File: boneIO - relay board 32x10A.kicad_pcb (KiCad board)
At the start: 2 copper layers, 197 x 102 mm, 120 parts, among them J1 Screw_Terminal_01x03, J10 Screw_Terminal_01x03, J11 Screw_Terminal_01x03, J12 Conn_02x04_Odd_Even, J13 Screw_Terminal_01x03, J14 Screw_Terminal_01x03, J15 Screw_Terminal_01x03, J16 Screw_Terminal_01x03, J17 Screw_Terminal_01x03, J2 Screw_Terminal_01x03, J3 Screw_Terminal_01x03, J4 Screw_Terminal_01x03, J5 Screw_Terminal_01x03, J6 Screw_Terminal_01x03, J7 Screw_Terminal_01x03, J8 Screw_Terminal_01x03, J9 Screw_Terminal_01x03, K1 HF32F/024-ZS3, K10 HF32F/024-ZS3, K11 HF32F/024-ZS3, K12 HF32F/024-ZS3, K13 HF32F/024-ZS3, K14 HF32F/024-ZS3, K15 HF32F/024-ZS3, K16 HF32F/024-ZS3, K17 HF32F/024-ZS3, K18 HF32F/024-ZS3, K19 HF32F/024-ZS3, K2 HF32F/024-ZS3, K20 HF32F/024-ZS3, K21 HF32F/024-ZS3, K22 HF32F/024-ZS3, K23 HF32F/024-ZS3, K24 HF32F/024-ZS3, K25 HF32F/024-ZS3, K26 HF32F/024-ZS3, K27 HF32F/024-ZS3, K28 HF32F/024-ZS3, K29 HF32F/024-ZS3, K3 HF32F/024-ZS3, K30 HF32F/024-ZS3, K31 HF32F/024-ZS3, K32 HF32F/024-ZS3, K4 HF32F/024-ZS3, K5 HF32F/024-ZS3, K6 HF32F/024-ZS3, K7 HF32F/024-ZS3, K8 HF32F/024-ZS3, K9 HF32F/024-ZS3, SW1 SW_DIP_x03, SW2 SW_DIP_x03, SW3 SW_DIP_x03, U1 PCF8575, U10 LM75_MSOP, U2 ULN2803A, U3 MCP23017_SS, U4 ULN2803A, U5 PCF8575, U6 ULN2803A, U7 MCP23017_SS, U8 ULN2803A, U9 MCP9808_SO8

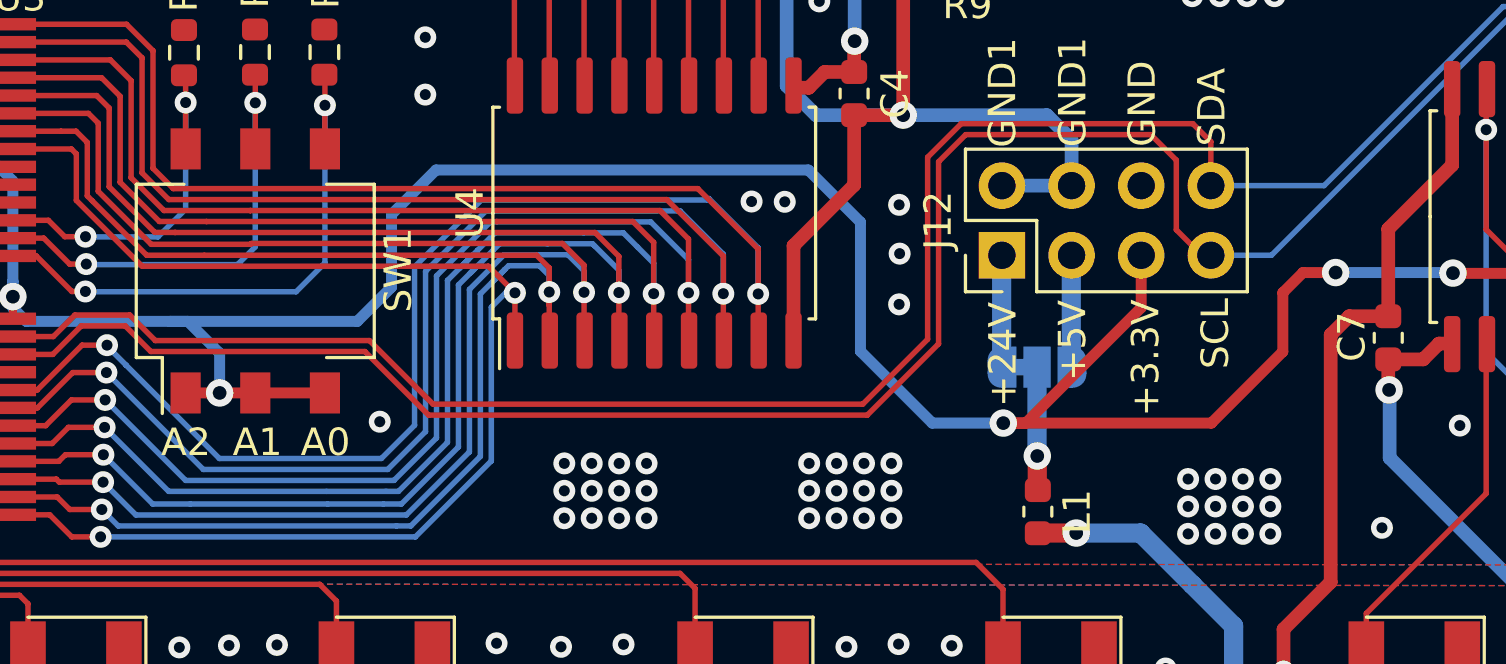
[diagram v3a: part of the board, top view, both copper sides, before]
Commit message: relay board 32x10A
Final Version
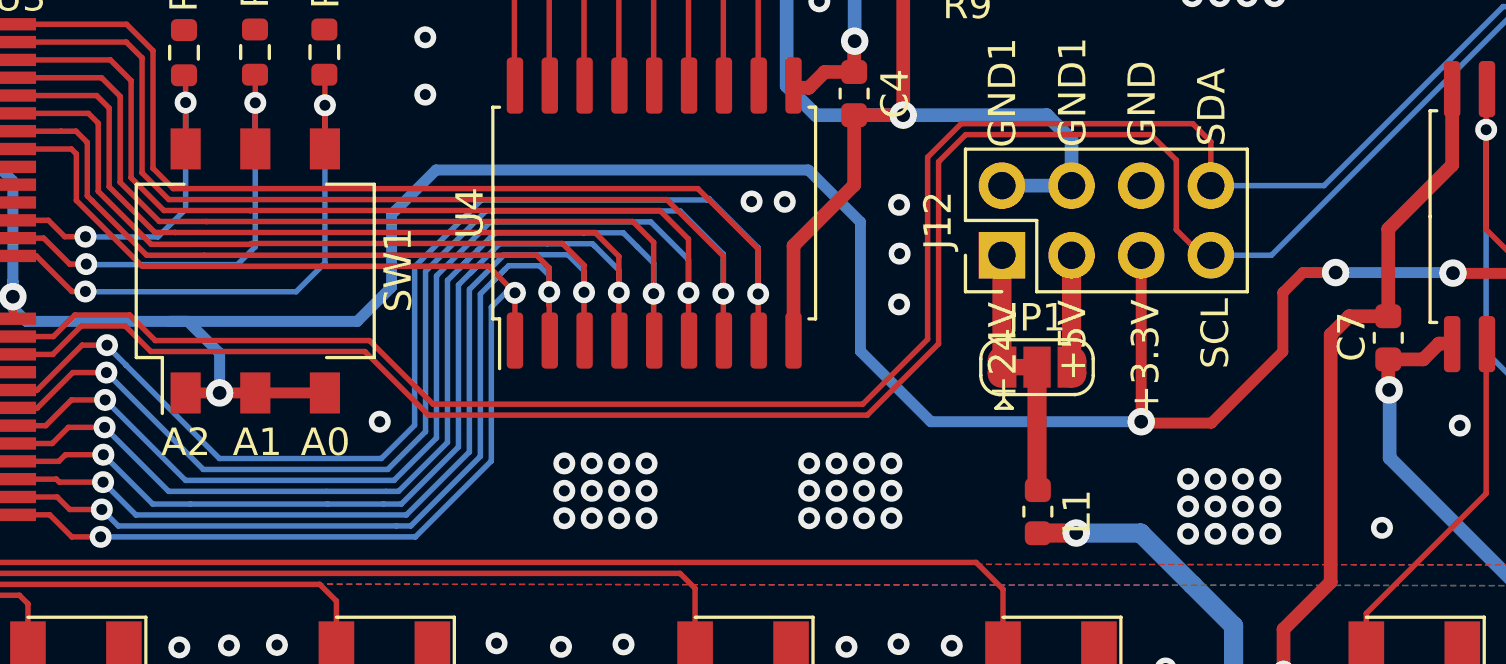
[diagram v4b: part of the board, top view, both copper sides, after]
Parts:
- JP1: moved to F.Cu
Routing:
- net +3V3: track 234.5 -> 231.9 mm
- net Net-(JP1-Pad2): vias 1 -> 0

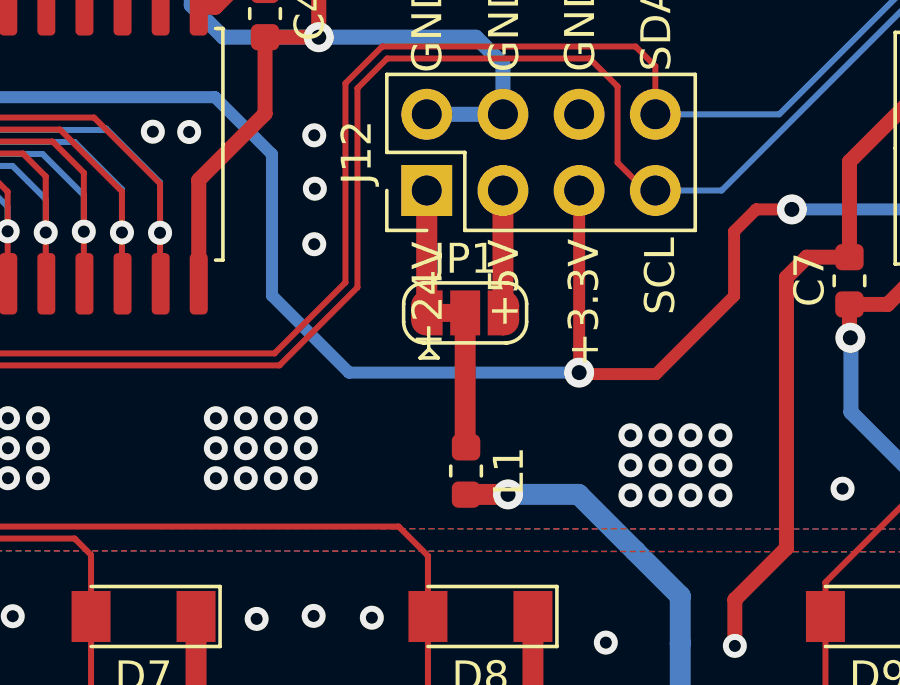
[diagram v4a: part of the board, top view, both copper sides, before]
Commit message: Update boneIO - relay board 32x10A.kicad_pcb
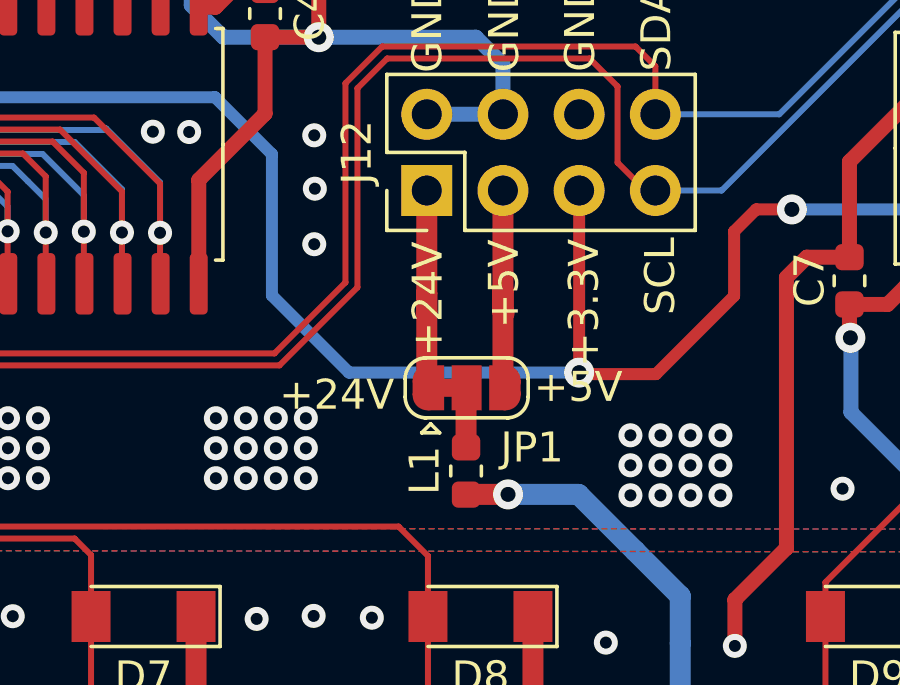
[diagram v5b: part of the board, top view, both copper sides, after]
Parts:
- moved JP1 2.50 mm to (379.5, 319.3)
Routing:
- net +5V: track 4.10 -> 7.38 mm
- net +24V: track 4.09 -> 7.26 mm
- net Net-(JP1-Pad2): track 4.49 -> 2.04 mm
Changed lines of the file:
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@@
   )
   (footprint "Jumper:SolderJumper-3_P1.3mm_Bridged12_RoundedPad1.0x1.5mm" (layer "F.Cu")
-    (at 379.43 316.798)
+    (at 379.48 319.2955)
     (descr "SMD Solder 3-pad Jumper, 1x1.5mm rounded Pads, 0.3mm gap, pads 1-2 bridged with 1 copper strip")
     (tags "net tie solder jumper bridged")
@@
     (property "Sheetname" "")
     (attr exclude_from_pos_files)
-    (fp_text reference "JP1" (at 0 -1.8) (layer "F.SilkS")
+    (fp_text reference "JP1" (at 2.18 1.9925) (layer "F.SilkS")
       (effects (font (size 1 1) (thickness 0.15)))
     )
@@
         (gr_circle (center 0 -0.25) (end 0.5 -0.25) (width 0) (fill yes))
         (gr_poly (pts
-            (xy 0.55 -0.75)
-            (xy 0 -0.75)
-            (xy 0 0.75)
             (xy 0.55 0.75)
+            (xy 0 0.75)
+            (xy 0 -0.75)
+            (xy 0.55 -0.75)
           ) (width 0) (fill yes))
       ))
@@
         (gr_circle (center 0 -0.25) (end 0.5 -0.25) (width 0) (fill yes))
         (gr_poly (pts
-            (xy 0 -0.75)
-            (xy -0.55 -0.75)
-            (xy -0.55 0.75)
             (xy 0 0.75)
+            (xy -0.55 0.75)
+            (xy -0.55 -0.75)
+            (xy 0 -0.75)
           ) (width 0) (fill yes))
       ))
@@
     (property "Sheetname" "")
     (attr smd)
-    (fp_text reference "L1" (at 0 -1.43 90) (layer "F.SilkS")
+    (fp_text reference "L1" (at -0.02 1.38 90) (layer "F.SilkS")
       (effects (font (size 1 1) (thickness 0.15)))
     )
@@
     (effects (font (size 0.8 0.8) (thickness 0.2)) (justify mirror))
   )
-  (gr_text "+24V" (at 375.1858 316.9436) (layer "B.SilkS")
-    (effects (font (size 1 1) (thickness 0.15)) (justify mirror))
-  )
   (gr_text "WARNING!!! " (at 315.84 309.383 -90) (layer "B.SilkS")
     (effects (font (size 1 1) (thickness 0.2)) (justify mirror))
   )
-  (gr_text "+5V" (at 383.3138 316.9436) (layer "B.SilkS")
-    (effects (font (size 1 1) (thickness 0.15)) (justify mirror))
-  )
   (gr_text "DOWN" (at 428.13 309.278 -90) (layer "B.SilkS")
     (effects (font (size 0.8 0.8) (thickness 0.2)) (justify mirror))
@@
     (effects (font (size 1 1) (thickness 0.15)))
   )
+  (gr_text "+24V" (at 375.15 319.528) (layer "F.SilkS")
+    (effects (font (size 1 1) (thickness 0.15)))
+  )
   (gr_text "J9" (at 471.58 272.108 -180) (layer "F.SilkS")
     (effects (font (size 1 1) (thickness 0.15)))
@@
     (effects (font (size 1 1) (thickness 0.15)))
   )
+  (gr_text "+5V" (at 383.2 319.268) (layer "F.SilkS")
+    (effects (font (size 1 1) (thickness 0.15)))
+  )
   (gr_text "J9" (at 423 272.128 -180) (layer "F.SilkS")
     (effects (font (size 1 1) (thickness 0.15)))
@@
   (segment (start 378.19 326.918) (end 378.19 330.468) (width 0.2) (layer "F.Cu") (net 12))
   (segment (start 378.15 316.778) (end 378.13 316.798) (width 0.7) (layer "F.Cu") (net 13))
-  (segment (start 378.15 312.718) (end 378.15 316.778) (width 0.7) (layer "F.Cu") (net 13))
+  (segment (start 378.15 319.2655) (end 378.18 319.2955) (width 0.7) (layer "F.Cu") (net 13))
+  (segment (start 378.15 316.138) (end 378.15 316.778) (width 0.7) (layer "F.Cu") (net 13))
+  (segment (start 378.15 312.718) (end 378.15 316.138) (width 0.7) (layer "F.Cu") (net 13))
+  (segment (start 378.15 316.138) (end 378.15 319.2655) (width 0.7) (layer "F.Cu") (net 13))
   (segment (start 338.346741 310.793) (end 338.070871 311.068871) (width 0.2) (layer "F.Cu") (net 14))
   (segment (start 338.070871 311.068871) (end 336.78 312.359741) (width 0.2) (layer "F.Cu") (net 14))
@@
   (segment (start 338.9395 312.4685) (end 339.25 312.158) (width 0.2) (layer "B.Cu") (net 16))
   (segment (start 344.756666 313.039224) (end 344.775442 313.058) (width 0.2) (layer "B.Cu") (net 16))
+  (segment (start 380.69 312.718) (end 380.69 316.048) (width 0.7) (layer "F.Cu") (net 17))
+  (segment (start 380.69 316.048) (end 380.69 316.758) (width 0.7) (layer "F.Cu") (net 17))
   (segment (start 380.69 316.758) (end 380.73 316.798) (width 0.7) (layer "F.Cu") (net 17))
-  (segment (start 380.69 312.718) (end 380.69 316.758) (width 0.7) (layer "F.Cu") (net 17))
+  (segment (start 380.69 316.048) (end 380.69 319.2055) (width 0.7) (layer "F.Cu") (net 17))
+  (segment (start 380.69 319.2055) (end 380.78 319.2955) (width 0.7) (layer "F.Cu") (net 17))
   (segment (start 339.36 313.228) (end 339.845 312.743) (width 0.2) (layer "F.Cu") (net 18))
   (segment (start 353.46 306.153) (end 353.44 306.133) (width 0.2) (layer "F.Cu") (net 18))
@@
   (segment (start 450.7 310.328) (end 448.21 312.818) (width 0.5) (layer "B.Cu") (net 140))
   (segment (start 370.3 306.538) (end 370.3 300.678) (width 0.5) (layer "B.Cu") (net 140))
+  (segment (start 379.46 321.2805) (end 379.46 319.3155) (width 0.7) (layer "F.Cu") (net 141))
   (segment (start 379.43 321.2505) (end 379.46 321.2805) (width 0.7) (layer "F.Cu") (net 141))
-  (segment (start 379.43 316.798) (end 379.43 321.2505) (width 0.7) (layer "F.Cu") (net 141))
+  (segment (start 379.46 319.3155) (end 379.48 319.2955) (width 0.7) (layer "F.Cu") (net 141))
   (segment (start 464.3 309.794783) (end 464.3 307.888) (width 0.2) (layer "F.Cu") (net 142))
   (segment (start 464.48 309.974783) (end 464.3 309.794783) (width 0.2) (layer "F.Cu") (net 142))
